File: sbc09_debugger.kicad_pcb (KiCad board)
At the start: 2 copper layers, 61 x 71.1 mm, 7 parts, among them J1 Conn_02x10_Odd_Even, J2 Conn_02x10_Odd_Even, J3 Conn_02x25_Odd_Even

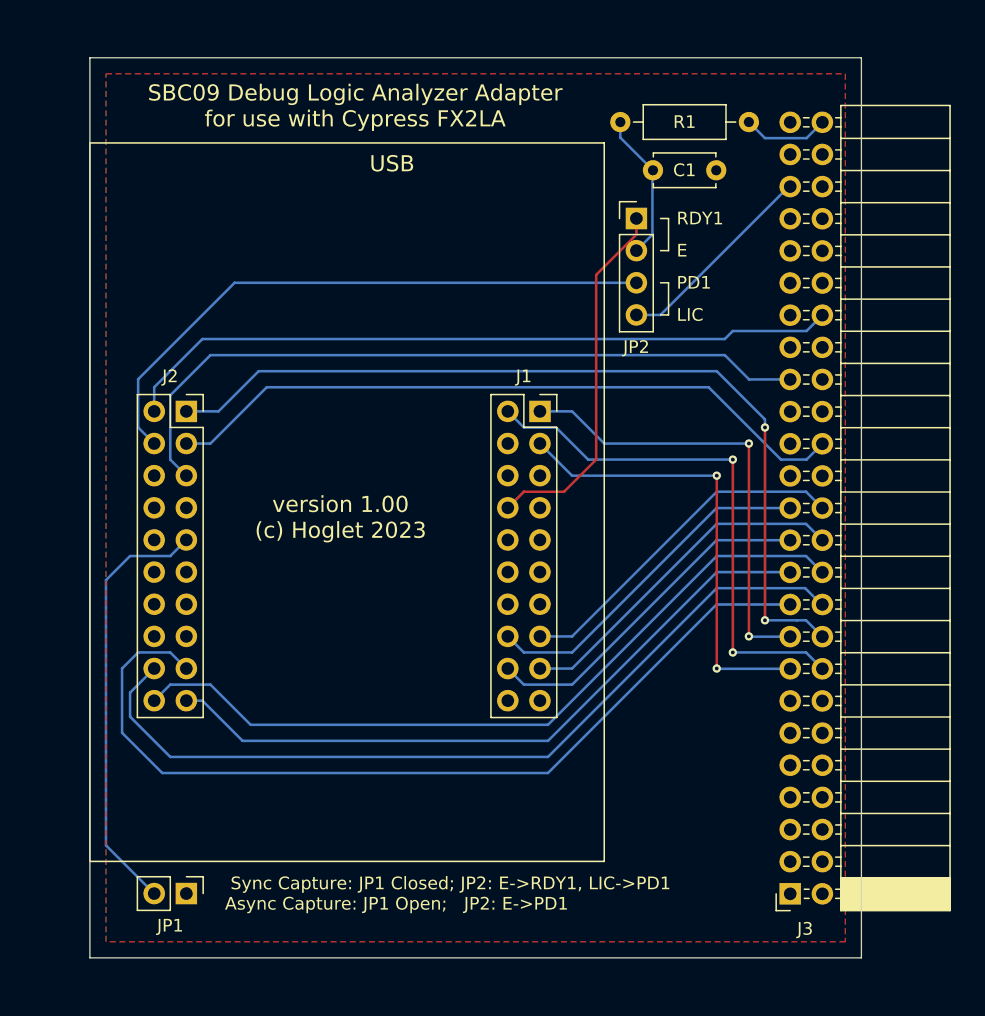
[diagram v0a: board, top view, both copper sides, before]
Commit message: Use backplane pin numbering and the correct male IDC footprint
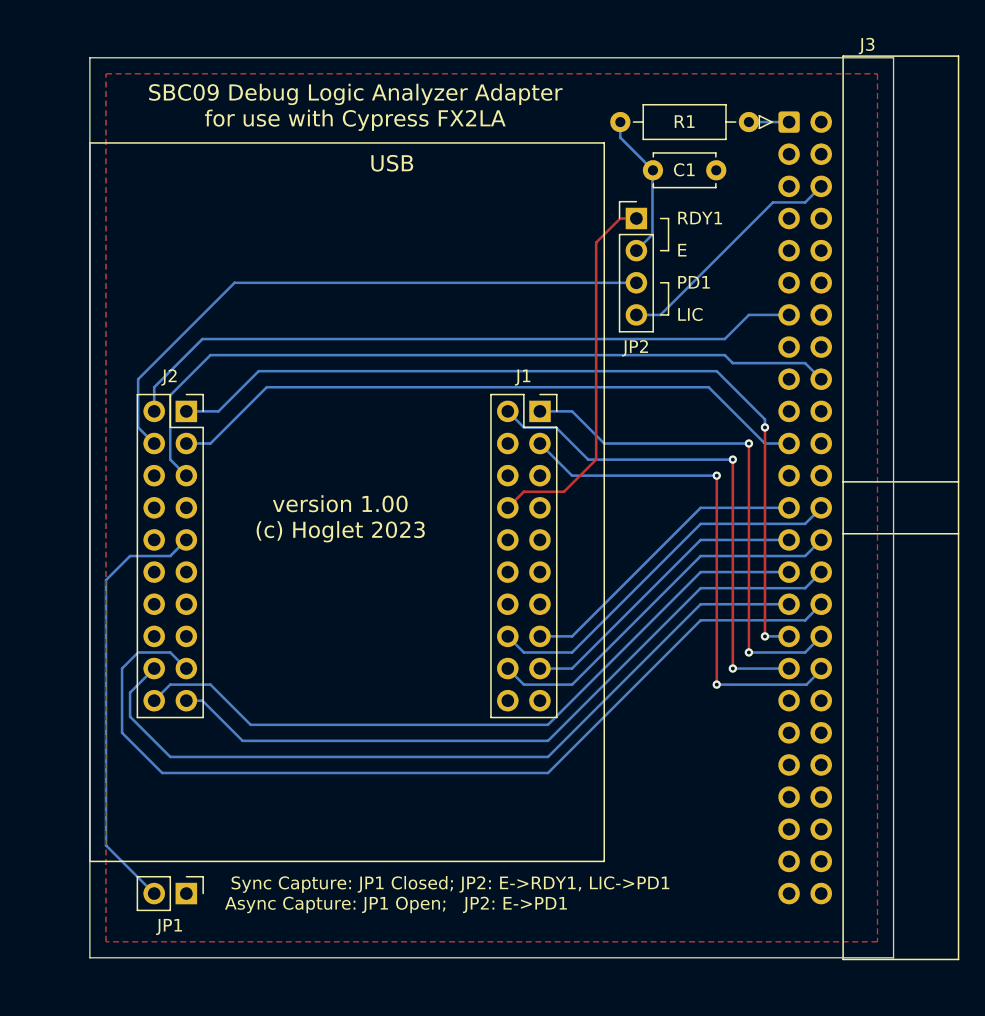
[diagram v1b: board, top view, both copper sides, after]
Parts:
- J3: footprint Connector_PinSocket_2.54mm:PinSocket_2x25_P2.54mm_Horizontal -> Connector_IDC:IDC-Header_2x25_P2.54mm_Horizontal
- moved J3 61.0 mm to (182.2, 71.1), turned to 0 degrees
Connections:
- J3 pad 1: GND -> Net-(J3-Pad1)
- J3 pad 13: unconnected-(J3-Pad13) -> BA
- J3 pad 15: A3 -> unconnected-(J3-Pad15)
- J3 pad 16: A2 -> unconnected-(J3-Pad16)
- J3 pad 17: A1 -> unconnected-(J3-Pad17)
- J3 pad 18: A0 -> RnW
- J3 pad 19: D7 -> unconnected-(J3-Pad19)
- J3 pad 20: D6 -> unconnected-(J3-Pad20)
- J3 pad 21: D5 -> BS
- J3 pad 22: D4 -> unconnected-(J3-Pad22)
- J3 pad 23: D3 -> unconnected-(J3-Pad23)
- J3 pad 24: D2 -> unconnected-(J3-Pad24)
- J3 pad 25: D1 -> D0
- J3 pad 26: D0 -> D1
- J3 pad 27: unconnected-(J3-Pad27) -> D2
- J3 pad 28: unconnected-(J3-Pad28) -> D3
- J3 pad 29: unconnected-(J3-Pad29) -> D4
- J3 pad 3: unconnected-(J3-Pad3) -> GND
- J3 pad 30: BS -> D5
- J3 pad 31: unconnected-(J3-Pad31) -> D6
- J3 pad 32: unconnected-(J3-Pad32) -> D7
- J3 pad 33: RnW -> A0
- J3 pad 34: unconnected-(J3-Pad34) -> A1
- J3 pad 35: unconnected-(J3-Pad35) -> A2
- J3 pad 36: unconnected-(J3-Pad36) -> A3
- J3 pad 38: BA -> unconnected-(J3-Pad38)
- J3 pad 4: unconnected-(J3-Pad4) -> GND
- J3 pad 45: LIC -> unconnected-(J3-Pad45)
- J3 pad 47: GND -> unconnected-(J3-Pad47)
- J3 pad 48: GND -> unconnected-(J3-Pad48)
- J3 pad 50: Net-(J3-Pad50) -> GND
- J3 pad 6: unconnected-(J3-Pad6) -> LIC
- R1 pad 1: Net-(J3-Pad50) -> Net-(J3-Pad1)
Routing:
- net Net-(J1-Pad8): track 0.00 -> 29.7 mm
- net /E: track 40.7 -> 11.7 mm
- net Net-(J3-Pad50): track 6.85 -> 0.00 mm
- net A3: track 36.1 -> 40.4 mm
- net A1: track 36.1 -> 40.3 mm
- net D4: track 60.7 -> 57.0 mm
- net D0: track 27.6 -> 23.9 mm
- net D2: track 27.6 -> 23.9 mm
- net D6: track 66.7 -> 63.0 mm
- net BS: track 55.0 -> 51.3 mm
- net Net-(J3-Pad1): track 0.00 -> 3.18 mm
- net BA: track 57.1 -> 54.4 mm
- net D1: track 27.6 -> 30.0 mm
- net LIC: track 16.4 -> 18.8 mm
- net D3: track 27.6 -> 30.0 mm
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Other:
- board size 61 x 71.1 mm -> 63.5 x 71.1 mm

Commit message: Move R1/C1 slightly
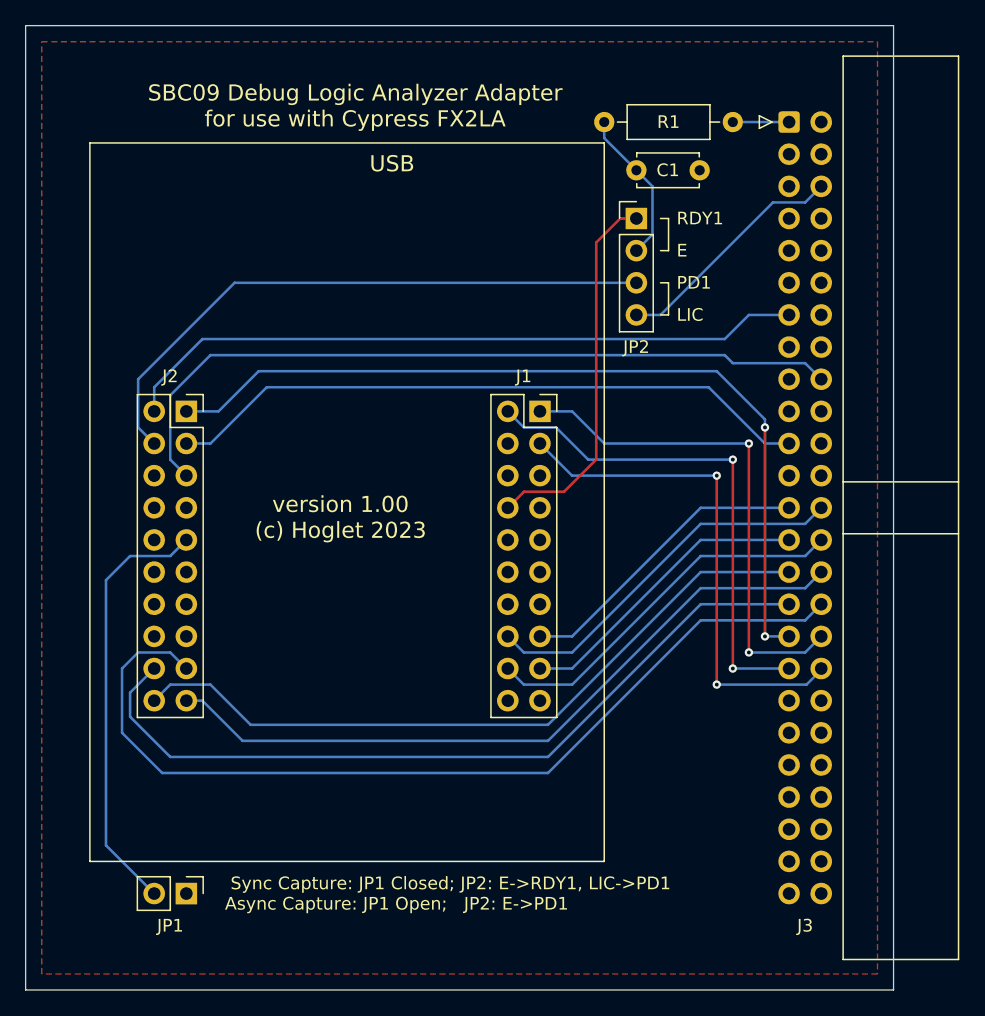
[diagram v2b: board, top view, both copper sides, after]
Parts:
- moved C1 1.31 mm to (170.2, 74.9)
- moved R1 1.27 mm to (177.8, 71.1)
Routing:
- net Net-(J3-Pad1): track 3.18 -> 4.44 mm
- net /E: track 11.7 -> 12.3 mm
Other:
- board size 63.5 x 71.1 mm -> 68.6 x 76.2 mm
- rule pad_to_mask_clearance: 0.1 -> 0.0508
- rule solder_mask_min_width: 0.2 -> 0.1016
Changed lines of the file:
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@@
       (dielectric_constraints no)
     )
-    (pad_to_mask_clearance 0.1)
-    (solder_mask_min_width 0.2)
+    (pad_to_mask_clearance 0.0508)
+    (solder_mask_min_width 0.1016)
     (pcbplotparams
-      (layerselection 0x00010fc_ffffffff)
+      (layerselection 0x00010f0_ffffffff)
       (disableapertmacros false)
-      (usegerberextensions false)
-      (usegerberattributes true)
-      (usegerberadvancedattributes true)
-      (creategerberjobfile true)
+      (usegerberextensions true)
+      (usegerberattributes false)
+      (usegerberadvancedattributes false)
+      (creategerberjobfile false)
       (svguseinch false)
       (svgprecision 6)
@@
       (psa4output false)
       (plotreference true)
-      (plotvalue true)
+      (plotvalue false)
       (plotinvisibletext false)
       (sketchpadsonfab false)
-      (subtractmaskfromsilk false)
+      (subtractmaskfromsilk true)
       (outputformat 1)
       (mirror false)
-      (drillshape 1)
+      (drillshape 0)
       (scaleselection 1)
-      (outputdirectory "")
+      (outputdirectory "manufacturing")
     )
   )
@@
   )
   (footprint "Capacitor_THT:C_Disc_D4.7mm_W2.5mm_P5.00mm" (layer "F.Cu")
-    (at 171.49 74.93)
+    (at 170.18 74.93)
     (descr "C, Disc series, Radial, pin pitch=5.00mm, , diameter*width=4.7*2.5mm^2, Capacitor, http://www.vishay.com/docs/45233/krseries.pdf")
     (tags "C Disc series Radial pin pitch 5.00mm  diameter 4.7mm width 2.5mm Capacitor")
@@
     (property "Sheetname" "")
     (attr through_hole)
-    (fp_text reference "J3" (at 6.215 -6.1) (layer "F.SilkS")
+    (fp_text reference "J3" (at 1.27 63.5) (layer "F.SilkS")
       (effects (font (size 1 1) (thickness 0.15)))
     )
@@
     (fp_line (start 13.28 -5.1) (end 13.28 66.06) (layer "F.Fab") (width 0.1))
     (fp_line (start -0.32 56.2) (end 4.38 56.2) (layer "F.Fab") (width 0.1))
-    (pad "1" thru_hole roundrect (at 0 0) (size 1.7 1.7) (drill 1) (layers *.Cu *.Mask) (roundrect_rratio 0.147059)
+    (pad "1" thru_hole roundrect (at 0 0) (size 1.7 1.7) (drill 1) (layers *.Cu *.Mask) (roundrect_rratio 0.1470588235)
       (net 55 "Net-(J3-Pad1)") (pinfunction "Pin_1") (pintype "passive"))
     (pad "2" thru_hole circle (at 2.54 0) (size 1.7 1.7) (drill 1) (layers *.Cu *.Mask)
@@
   )
   (footprint "Resistor_THT:R_Axial_DIN0207_L6.3mm_D2.5mm_P10.16mm_Horizontal" (layer "F.Cu")
-    (at 179.07 71.12 180)
+    (at 177.8 71.12 180)
     (descr "Resistor, Axial_DIN0207 series, Axial, Horizontal, pin pitch=10.16mm, 0.25W = 1/4W, length*diameter=6.3*2.5mm^2, http://cdn-reichelt.de/documents/datenblatt/B400/1_4W%23YAG.pdf")
     (tags "Resistor Axial_DIN0207 series Axial Horizontal pin pitch 10.16mm 0.25W = 1/4W length 6.3mm diameter 2.5mm")
@@
   (gr_line (start 172.085 78.74) (end 172.72 78.74) (layer "F.SilkS") (width 0.12))
   (gr_rect (start 127 129.54) (end 167.64 72.771) (layer "F.SilkS") (width 0.12) (fill none))
-  (gr_rect (start 127 66.04) (end 190.5 137.16) (layer "Edge.Cuts") (width 0.05) (fill none))
+  (gr_rect (start 121.92 63.5) (end 190.5 139.7) (layer "Edge.Cuts") (width 0.05) (fill none))
   (gr_text "LIC" (at 173.355 86.36) (layer "F.SilkS")
     (effects (font (size 1 1) (thickness 0.15)) (justify left))
@@
     (effects (font (size 1 1) (thickness 0.15)) (justify left))
   )
-  (segment (start 171.45 80.01) (end 171.45 74.97) (width 0.2032) (layer "B.Cu") (net 1))
+  (segment (start 171.45 80.01) (end 171.45 76.2) (width 0.2032) (layer "B.Cu") (net 1))
+  (segment (start 167.64 72.39) (end 170.18 74.93) (width 0.2032) (layer "B.Cu") (net 1))
+  (segment (start 171.45 76.2) (end 170.18 74.93) (width 0.2032) (layer "B.Cu") (net 1))
+  (segment (start 167.64 71.12) (end 167.64 72.39) (width 0.2032) (layer "B.Cu") (net 1))
   (segment (start 170.18 81.28) (end 171.45 80.01) (width 0.2032) (layer "B.Cu") (net 1))
-  (segment (start 168.91 71.12) (end 168.91 72.35) (width 0.2032) (layer "B.Cu") (net 1))
-  (segment (start 168.91 72.35) (end 171.49 74.93) (width 0.2032) (layer "B.Cu") (net 1))
   (segment (start 176.53 115.57) (end 176.53 99.06) (width 0.2032) (layer "F.Cu") (net 8))
   (via (at 176.53 99.06) (size 0.6604) (drill 0.3048) (layers "F.Cu" "B.Cu") (net 8))
@@
   (segment (start 130.81 91.44) (end 138.43 83.82) (width 0.2032) (layer "B.Cu") (net 54))
   (segment (start 132.08 96.52) (end 130.81 95.25) (width 0.2032) (layer "B.Cu") (net 54))
-  (segment (start 179.07 71.12) (end 182.245 71.12) (width 0.2032) (layer "B.Cu") (net 55))
+  (segment (start 177.8 71.12) (end 182.245 71.12) (width 0.2032) (layer "B.Cu") (net 55))
   (zone (net 2) (net_name "GND") (layer "F.Cu") (hatch edge 0.508)
     (connect_pads (clearance 0.508))
@@
     (polygon
       (pts
-        (xy 189.23 135.89)
-        (xy 128.27 135.89)
-        (xy 128.27 67.31)
-        (xy 189.23 67.31)
+        (xy 189.23 138.43)
+        (xy 123.19 138.43)
+        (xy 123.19 64.77)
+        (xy 189.23 64.77)
       )
     )
